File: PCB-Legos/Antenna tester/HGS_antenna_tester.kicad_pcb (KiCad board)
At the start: 4 copper layers, 100 x 100 mm, 12 parts, among them J1 Conn_Coaxial, J2 Conn_01x01

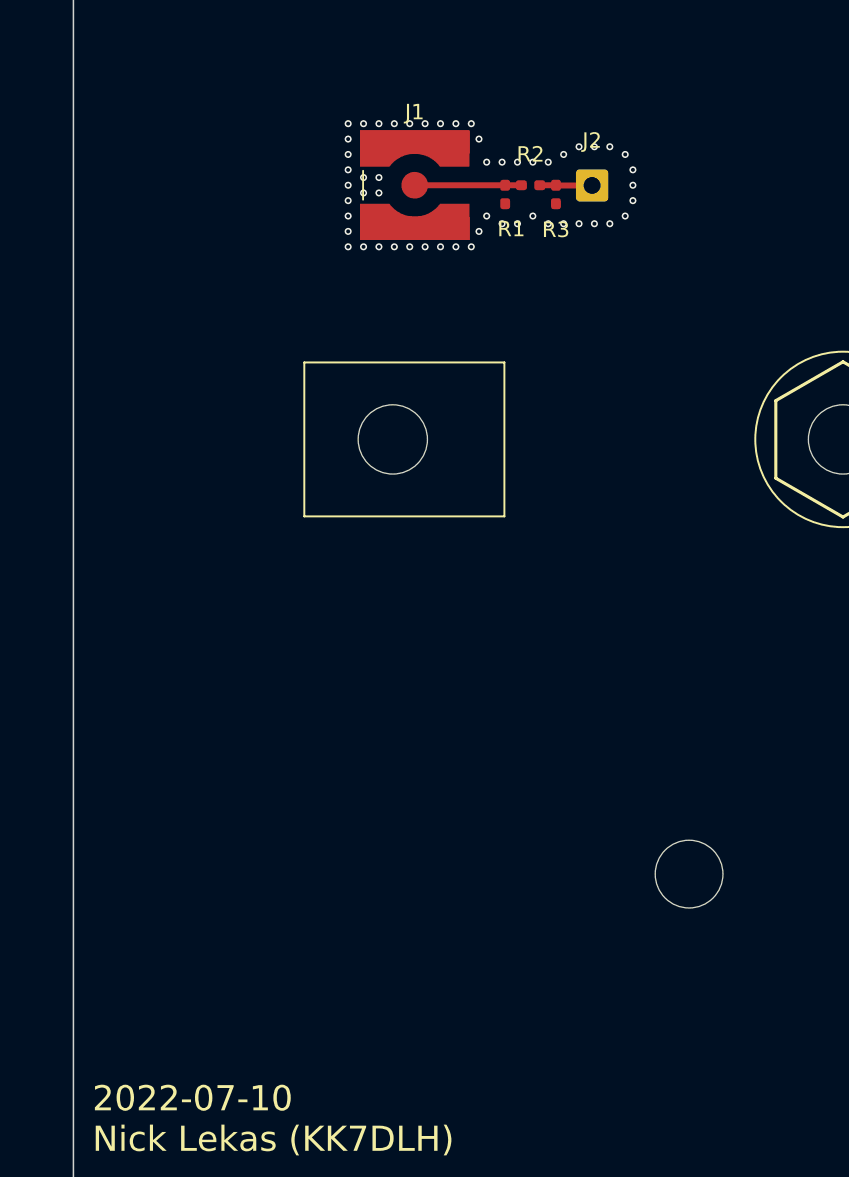
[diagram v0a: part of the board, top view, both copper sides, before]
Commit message: pulled refdes's away from stiching
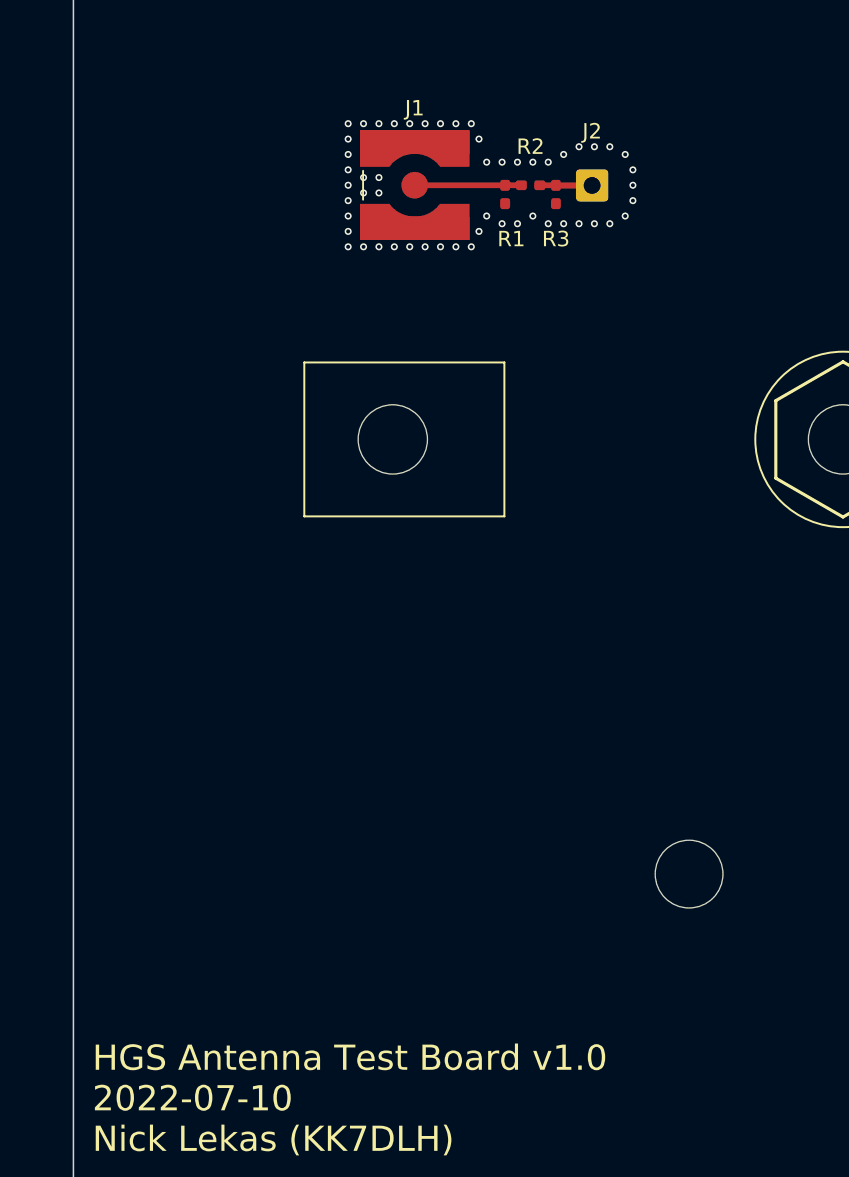
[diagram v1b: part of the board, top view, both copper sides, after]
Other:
- board text added: "HGS Antenna Test Board v1.0 2022-07-10 Nick Lekas (KK7DLH)"
- board text removed: "2022-07-10 Nick Lekas (KK7DLH)"
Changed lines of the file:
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@@
     (property "Sheetname" "")
     (attr exclude_from_pos_files)
-    (fp_text reference "J2" (at 0 -2.9135) (layer "F.SilkS")
+    (fp_text reference "J2" (at 0 -3.5135) (layer "F.SilkS")
       (effects (font (size 1 1) (thickness 0.15)))
     )
@@
     (property "Sheetname" "")
     (attr smd)
-    (fp_text reference "J1" (at 0 -4.75) (layer "F.SilkS")
+    (fp_text reference "J1" (at 0 -5) (layer "F.SilkS")
       (effects (font (size 1 1) (thickness 0.15)))
     )
@@
     (property "Sheetname" "")
     (attr smd)
-    (fp_text reference "R3" (at 2.3 0 180) (layer "F.SilkS")
+    (fp_text reference "R3" (at 2.9 0 180) (layer "F.SilkS")
       (effects (font (size 1 1) (thickness 0.15)))
     )
@@
     (property "Sheetname" "")
     (attr smd)
-    (fp_text reference "R2" (at 0 -2) (layer "F.SilkS")
+    (fp_text reference "R2" (at 0 -2.5) (layer "F.SilkS")
       (effects (font (size 1 1) (thickness 0.15)))
     )
@@
     (property "Sheetname" "")
     (attr smd)
-    (fp_text reference "R1" (at 2.25 -0.4) (layer "F.SilkS")
+    (fp_text reference "R1" (at 2.9 -0.4) (layer "F.SilkS")
       (effects (font (size 1 1) (thickness 0.15)))
     )
@@
   (gr_circle (center 182.1511 56.5135) (end 187.6511 56.5135) (layer "B.CrtYd") (width 0.1) (fill none))
   (gr_circle (center 155.1511 101.5135) (end 161.1511 101.5135) (layer "F.CrtYd") (width 0.1) (fill none))
-  (gr_text "2022-07-10\nNick Lekas (KK7DLH)" (at 106.3811 147.9335) (layer "F.SilkS")
+  (gr_text "HGS Antenna Test Board v1.0\n2022-07-10\nNick Lekas (KK7DLH)" (at 106.3811 147.9335) (layer "F.SilkS")
     (effects (font (size 1.63576 1.63576) (thickness 0.14224)) (justify left bottom))
   )

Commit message: stictching and typo fixes
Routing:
- net GND: vias 54 -> 209
